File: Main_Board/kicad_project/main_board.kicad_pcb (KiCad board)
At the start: 4 copper layers, 150 x 120 mm, 241 parts, among them J1 MOTOR, J10 USB_B_Micro, J11 DATA_UART, J12 I2C_EXTERNAL, J13 DEBUG_HEADER, J14 IO1, J15 IO7, J16 IO2, J17 IO3, J18 IO8, J19 IO9, J2 MOTOR, J20 IO4, J21 IO5, J22 IO10, J23 IO6, J24 EXPANSION_HEADER, J3 MOTOR, J4 MOTOR, J5 PWR_ENTRY, J6 12V_HDR, J7 3V3_HDR, J8 5V_HDR, J9 I2C_BUFFERED, SW1 SW_SPST, U1 TMC2209, U2 TMC2209, U3 TMC2209, U4 TMC2209, U5 TPS562200, U6 TPS562200, U7 PCA9600DP, U8 USBLC6-2SC6, U9 STM32G474VxT, Y1 ABS06-32.768kHz, Y2 DNP

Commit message: Main board sch: add backup battery, update license
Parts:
- removed G***: LOGO, LoaDy:FI_LOGO_15x14mm
- removed G***: LOGO, LoaDy:EmLab_LOGO_13mm
- added BT1: CR2032, LoaDy:CR2032_SMD, B.Cu at (104.8, 102.8)
- moved SW1 14.8 mm to (116.9, 108.4)
- moved C68 14.8 mm to (125.8, 109.2)
- moved R22 14.8 mm to (128.2, 108.4)
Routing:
- net Net-(BT1-Pad1): track 0.00 -> 51.7 mm, vias 0 -> 1
- net /MCU/NRST: track 42.6 -> 29.0 mm
- net GND: vias 336 -> 345
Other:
- board text added: "+"
- board text added: "-"
- board text added: "12V GND"
- board text added: "12V INPUT"
- board text added: "Cube Main Board Revision 1 O. Pecák (@LoaDy588) October 2020"
- board text added: "GND 3V3"
- board text added: "GND 5V"
- board text added: "JLCJLCJLCJLC"
- board text added: "Licensed under CERN-OHL-W v2"
- board text removed: "Cube Main Board"
- board text removed: "Cube Main Board Revision 1 O. Pecák (LoaDy) September 2020"

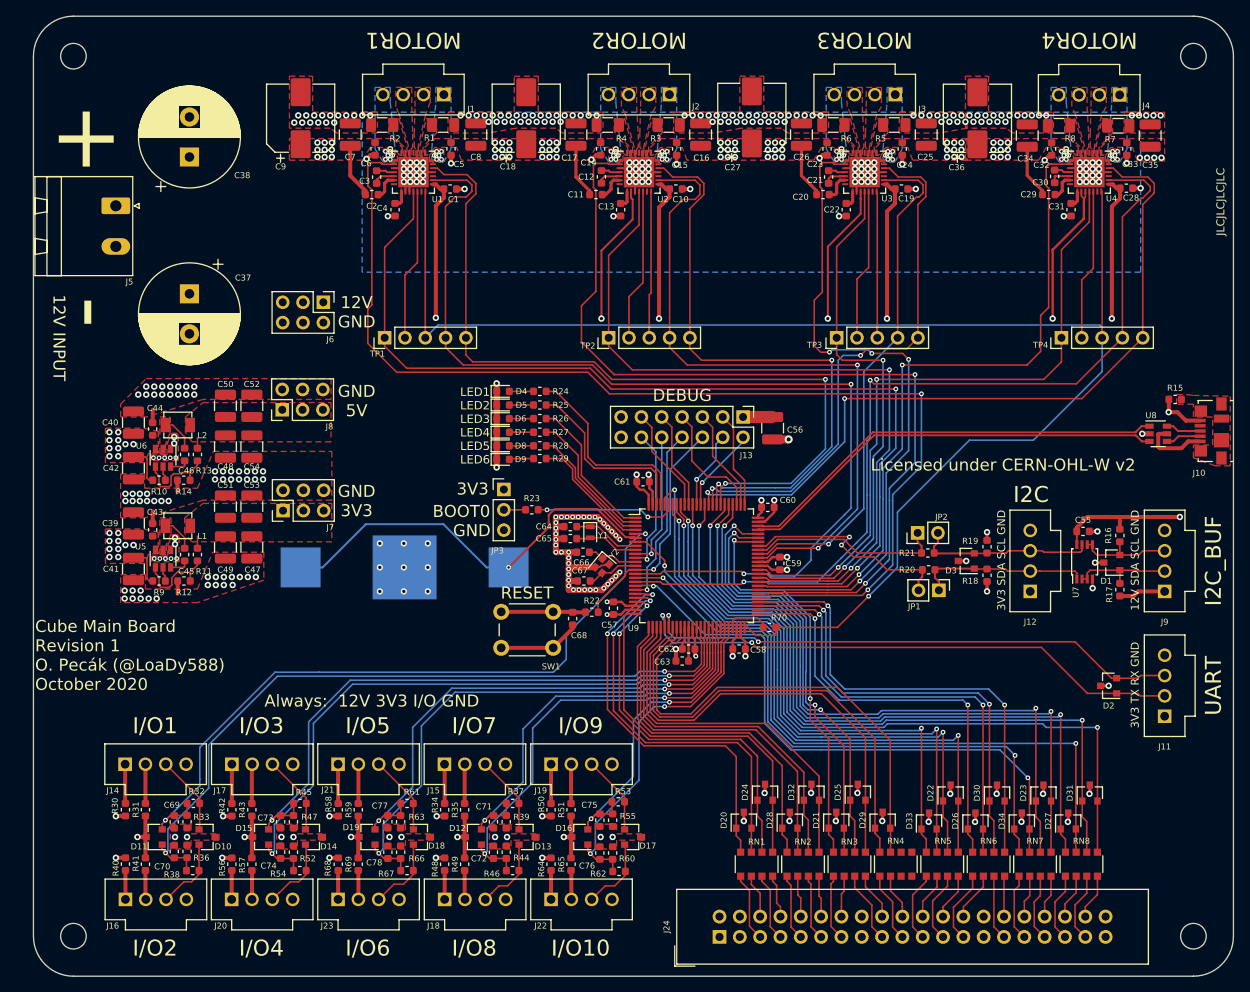
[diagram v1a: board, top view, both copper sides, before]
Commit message: change connector for interface board, edit silkscreen layers for interface and main boards
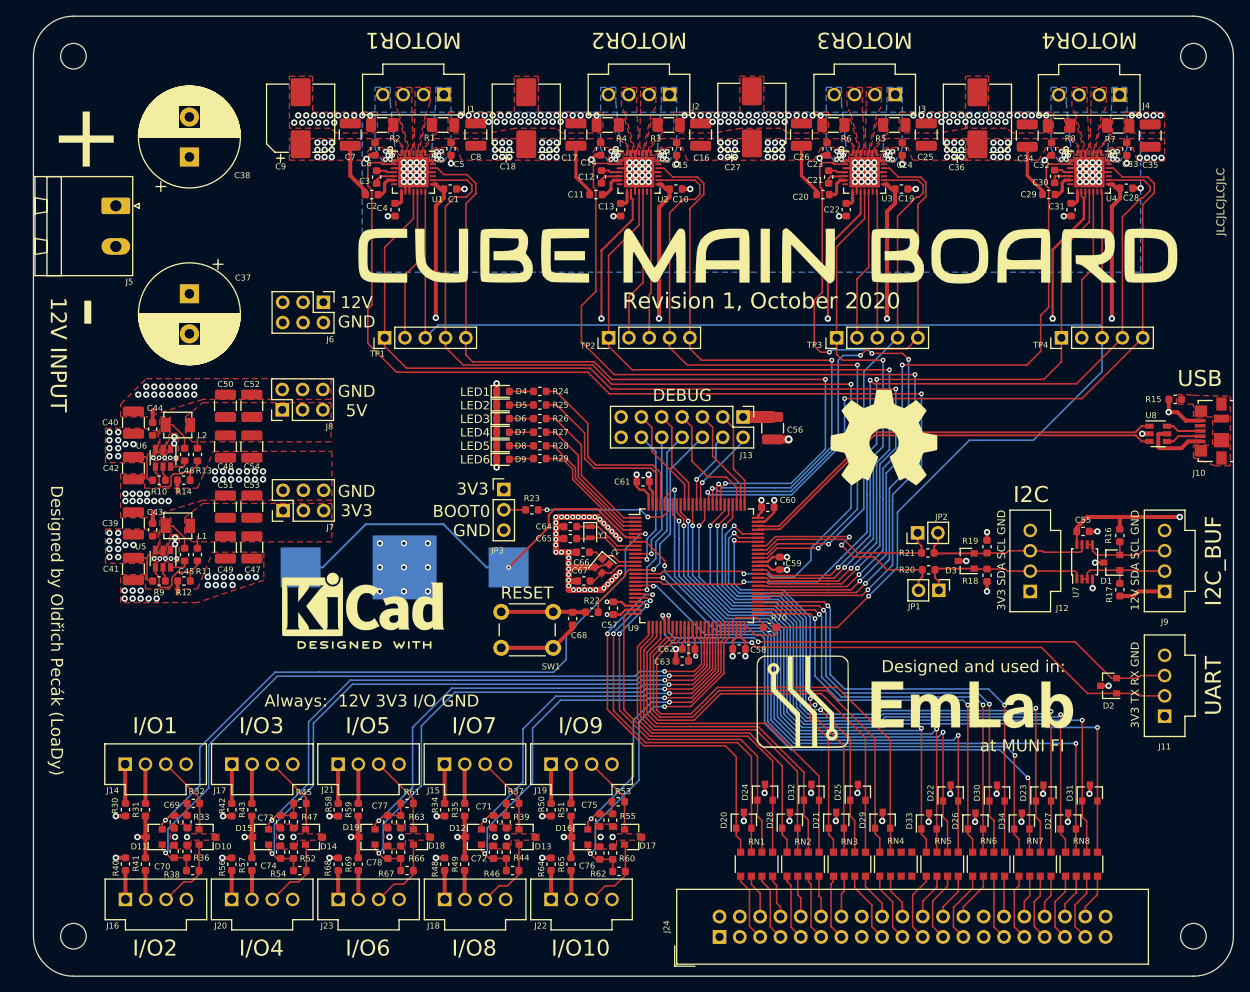
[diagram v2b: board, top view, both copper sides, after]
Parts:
- added G***: LOGO, kicad_project:logo_board, F.Cu at (150.2, 63.9)
- added G***: LOGO, LoaDy:EmLab_LOGO_11mm, F.Cu at (168.7, 119.6)
- added REF**: OSHW-Symbol_13.4x12mm_SilkScreen, Symbol:OSHW-Symbol_13.4x12mm_SilkScreen, F.Cu at (164.7, 86.6)
- added REF**: KiCad-Logo2_8mm_SilkScreen, Symbol:KiCad-Logo2_8mm_SilkScreen, F.Cu at (99.6, 107.4)
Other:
- board text added: "ATTACH HEATSINK!"
- board text added: "Cube Main Board Revision 1 Oldřich Pecák (LoaDy) Licensed under CERN-OHL-W v2 October 2020"
- board text added: "Designed and used in:"
- board text added: "Designed by Oldřich Pecák (LoaDy)"
- board text added: "RTC Back up battery CR2032"
- board text added: "Revision 1, October 2020"
- board text added: "Twitter and Github: LoaDy588 Repo: https://github.com/LoaDy588/cube_electronics"
- board text added: "USB"
- board text added: "at MUNI FI"
- board text removed: "Cube Main Board Revision 1 O. Pecák (@LoaDy588) October 2020"
- board text removed: "Licensed under CERN-OHL-W v2"

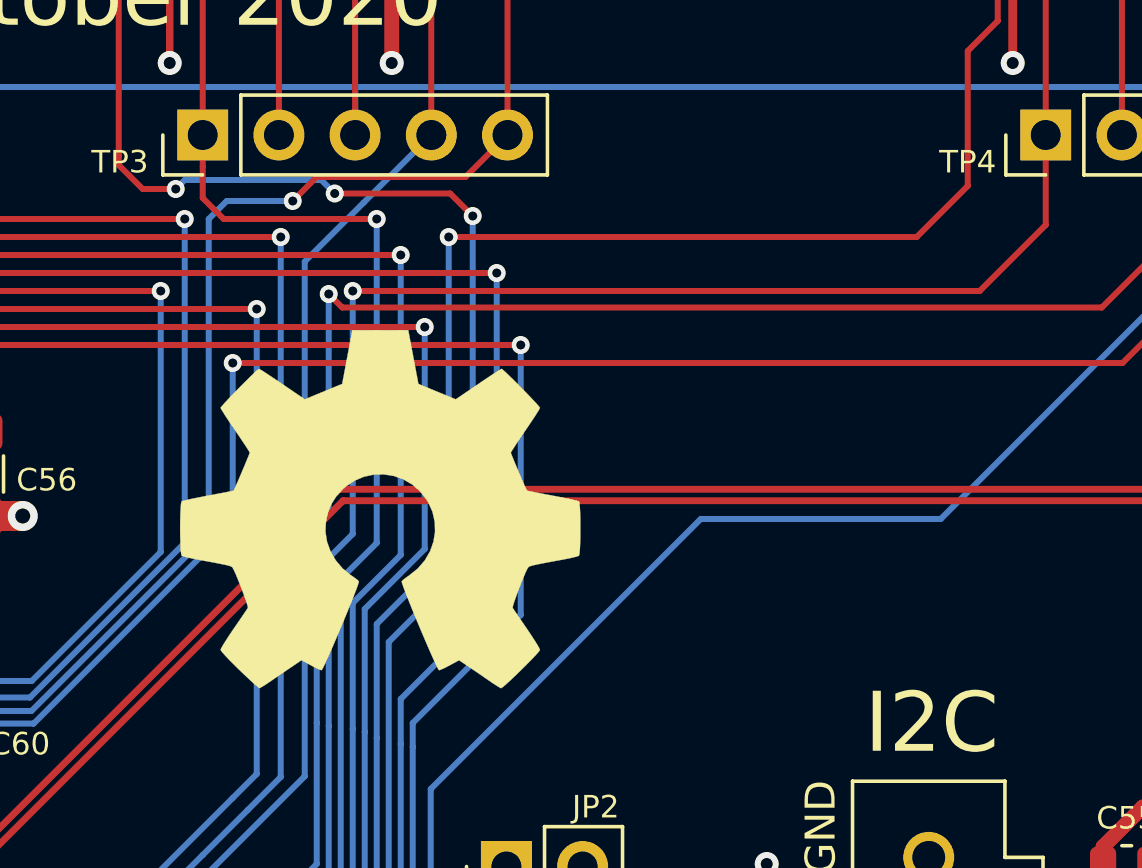
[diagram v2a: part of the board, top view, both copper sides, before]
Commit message: change oshw logo pos on mainboard
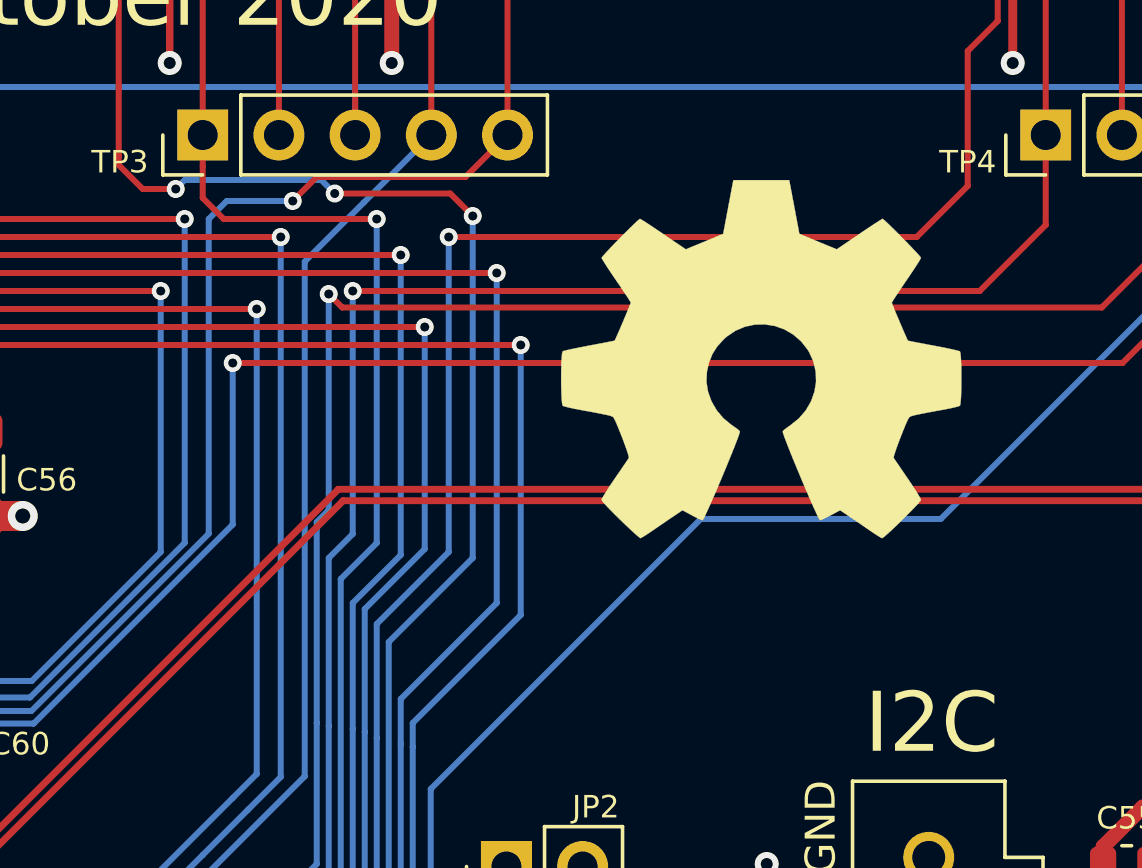
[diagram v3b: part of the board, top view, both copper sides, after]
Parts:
- moved REF** 13.6 mm to (177.4, 81.6)
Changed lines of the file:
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@@
   )
   (module Symbol:OSHW-Symbol_13.4x12mm_SilkScreen (layer F.Cu)
-    (at 164.7 86.6)
+    (at 177.4 81.6)
     (descr "Open Source Hardware Symbol")
     (tags "Logo Symbol OSHW")

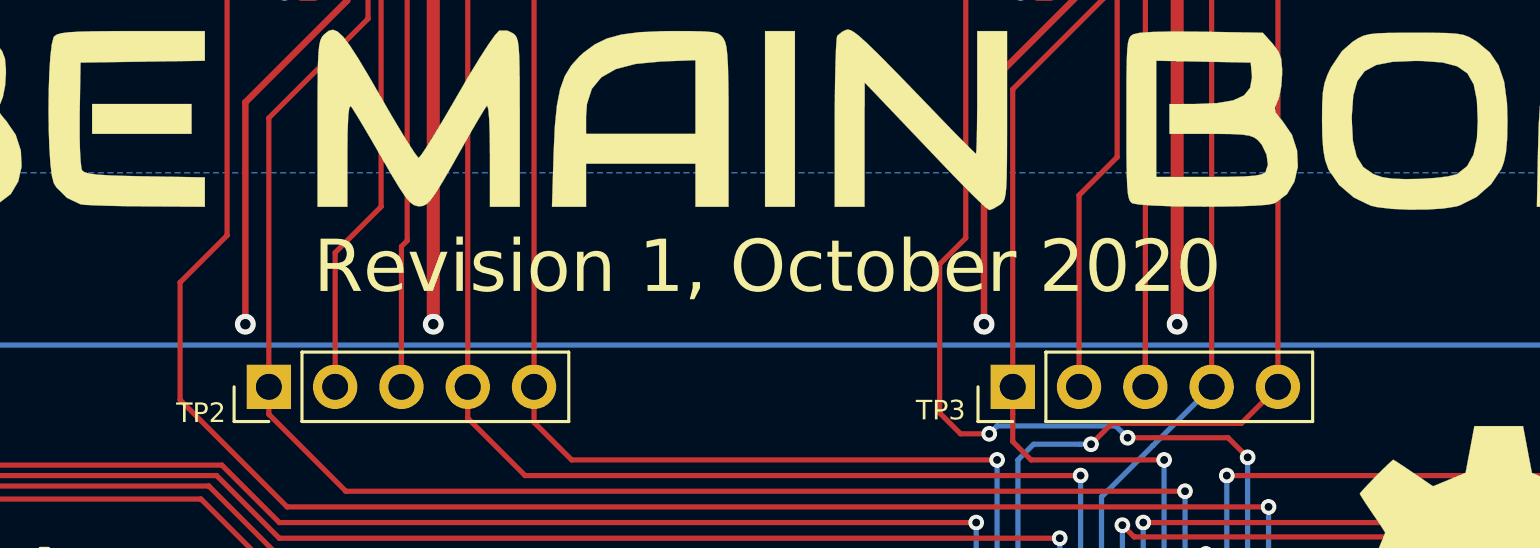
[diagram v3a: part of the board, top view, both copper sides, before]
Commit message: add interface board silkscreen, modify main board silkscreen
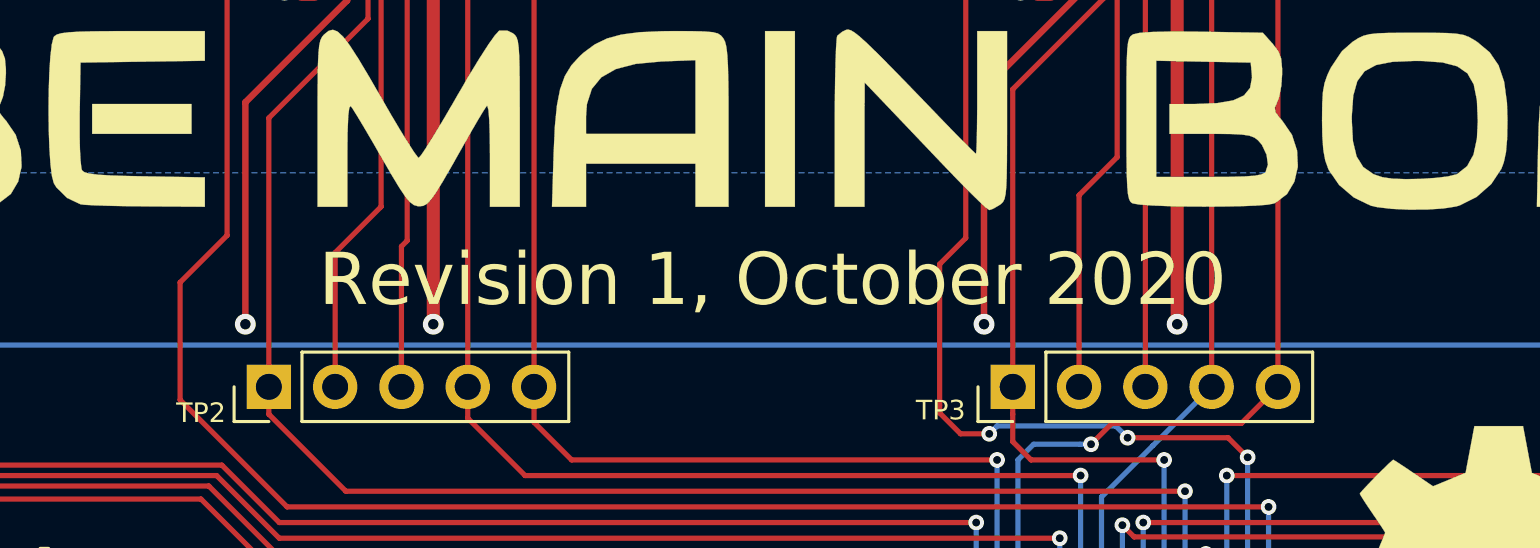
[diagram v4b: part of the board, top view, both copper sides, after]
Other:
- board text added: "Twitter and Github: LoaDy588 Repo: github.com/LoaDy588/cube_electronics"
- board text removed: "Twitter and Github: LoaDy588 Repo: https://github.com/LoaDy588/cube_electronics"
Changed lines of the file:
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@@
     (effects (font (size 1.5 1.5) (thickness 0.25)))
   )
-  (gr_text "Revision 1, October 2020" (at 149.4 69.5) (layer F.SilkS)
+  (gr_text "Revision 1, October 2020" (at 149.6 70) (layer F.SilkS)
     (effects (font (size 2 2) (thickness 0.4)))
   )
@@
     (effects (font (size 2 2) (thickness 0.4)) (justify mirror))
   )
-  (gr_text "Twitter and Github: LoaDy588\nRepo: https://github.com/LoaDy588/cube_electronics\n" (at 148.5 120.7) (layer B.SilkS)
+  (gr_text "Twitter and Github: LoaDy588\nRepo: github.com/LoaDy588/cube_electronics\n" (at 148.5 120.7) (layer B.SilkS)
     (effects (font (size 2 2) (thickness 0.3)) (justify left mirror))
   )
@@
         (xy 147.7 150) (xy 145.6 150) (xy 145.6 143.1) (xy 143.4 138.4) (xy 131.8 138.4)
         (xy 131.8 134.9) (xy 122.9 134.9) (xy 122.9 125) (xy 88.5 125) (xy 88.5 102.2)
-        (xy 88.5 91.3) (xy 96.4 86.8) (xy 96.4 71.2) (xy 197.3 71.2)
+        (xy 88.5 91.3) (xy 96.4 86.8) (xy 96.4 71.3) (xy 197.3 71.3)
       )
     )
